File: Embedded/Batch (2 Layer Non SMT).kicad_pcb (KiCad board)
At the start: 2 copper layers, 100 x 100 mm, 57 parts, among them J1 Conn_01x02_Socket, J1 Conn_01x03_Socket, J1 Conn_01x04_Socket, J1 HUB75, J1 S JST, J1 VL53L0X, J2 Conn_01x02_Socket, J2 Conn_01x04_Socket, J2 Conn_02x10_Odd_Even, J2 D0 FFC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

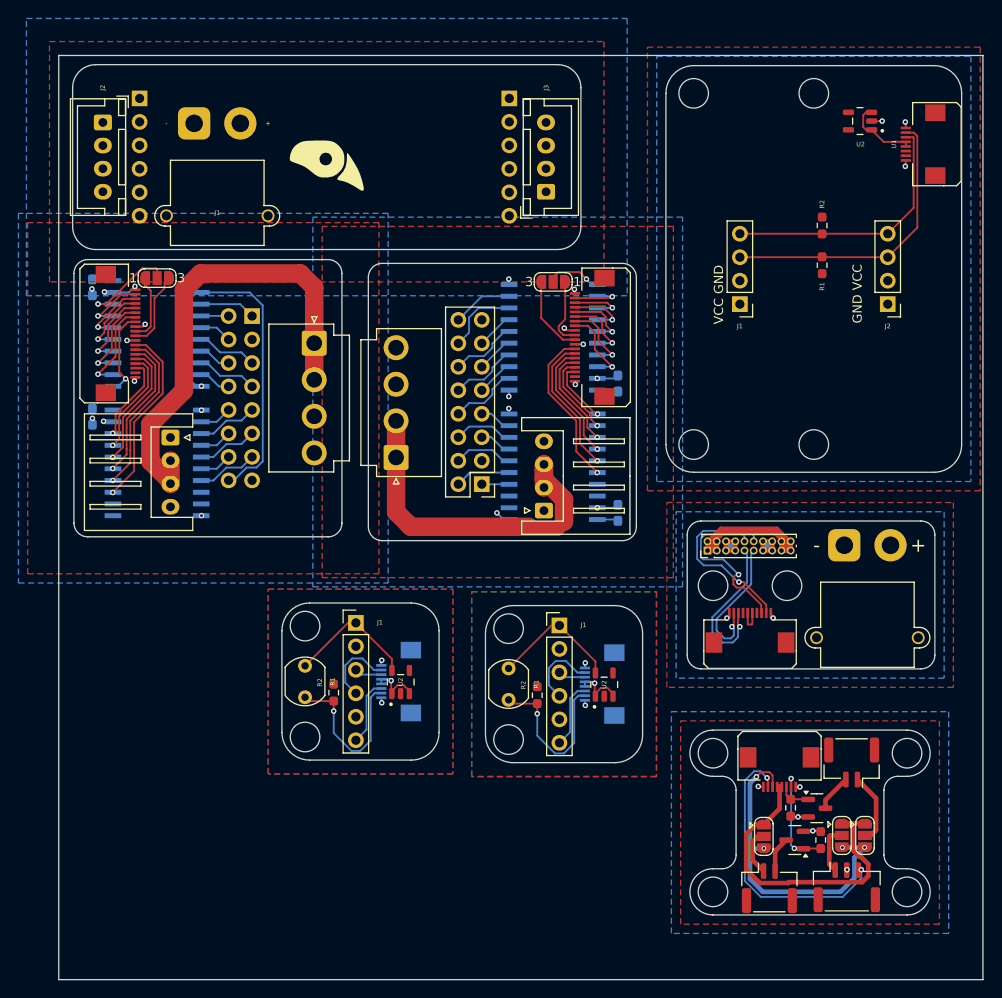
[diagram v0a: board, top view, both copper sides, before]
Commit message: Modified Board positions for optimal cutting & manufacture
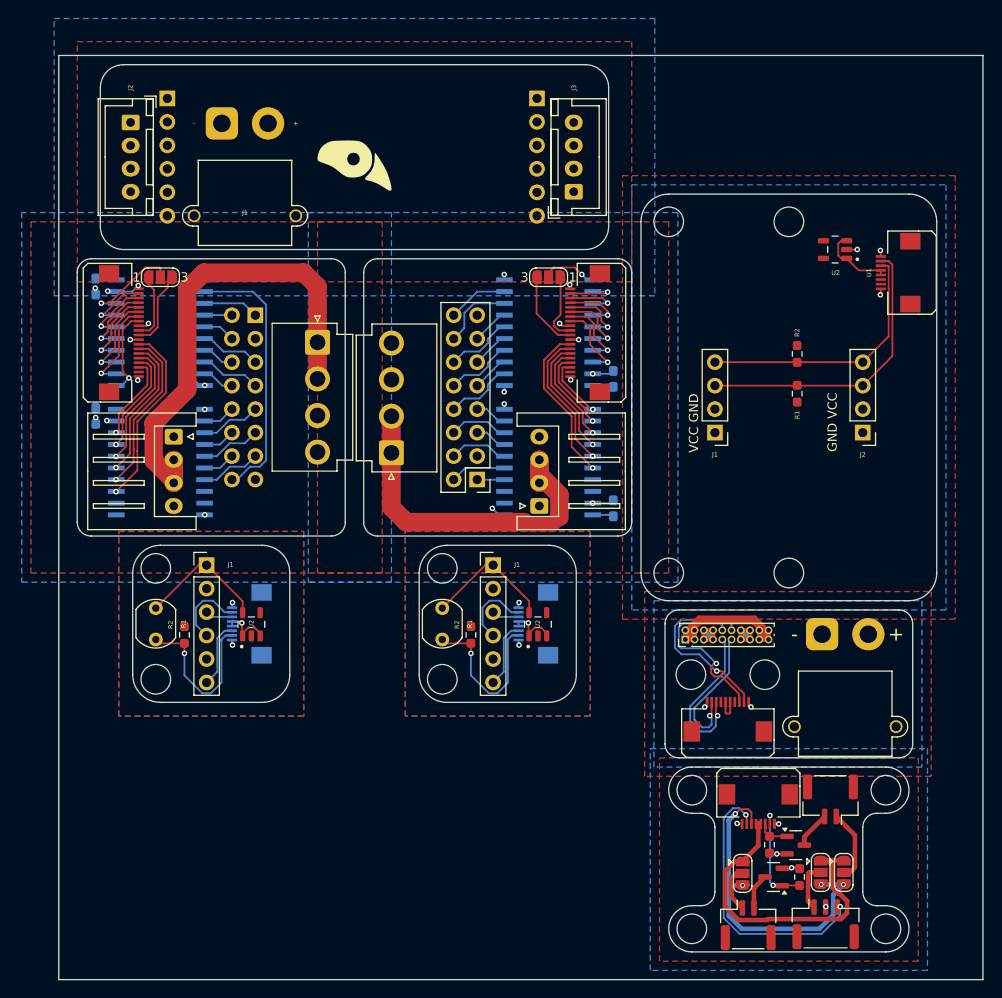
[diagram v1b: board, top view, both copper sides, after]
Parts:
- moved R1 17.3 mm to (40.5, 89.8)
- moved J1 17.3 mm to (46.0, 85.2)
- moved U1 17.3 mm to (49.4, 91.5)
- moved U2 17.3 mm to (50.8, 91.5)
- moved R2 17.3 mm to (43.6, 92.7)
- moved J1 14.2 mm to (101.0, 70.8)
- moved J2 14.2 mm to (117.0, 70.8)
- moved G*** 14.2 mm to (110.5, 66.5)
- moved U1 14.2 mm to (119.6, 53.5)
- moved U2 14.2 mm to (114.0, 51.0)
- moved R2 14.2 mm to (109.9, 62.3)
- moved R1 14.2 mm to (109.9, 66.6)
- moved J1 9.92 mm to (112.6, 92.6)
- moved J2 9.92 mm to (97.8, 93.2)
- moved G*** 9.92 mm to (115.4, 101.5)
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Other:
- outline, holes or cut-outs redrawn
